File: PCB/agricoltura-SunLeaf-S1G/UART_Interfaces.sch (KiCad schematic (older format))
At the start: 8 parts

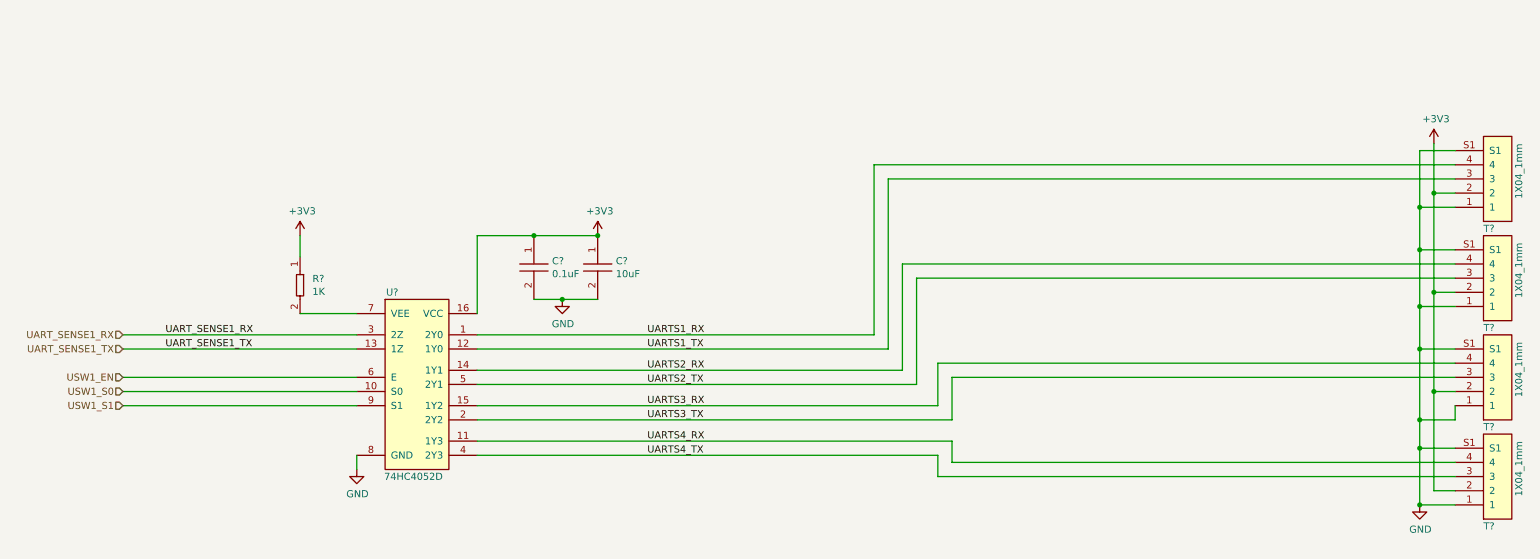
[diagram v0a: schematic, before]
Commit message: Schematic Complete
Schematic completed and PCB started
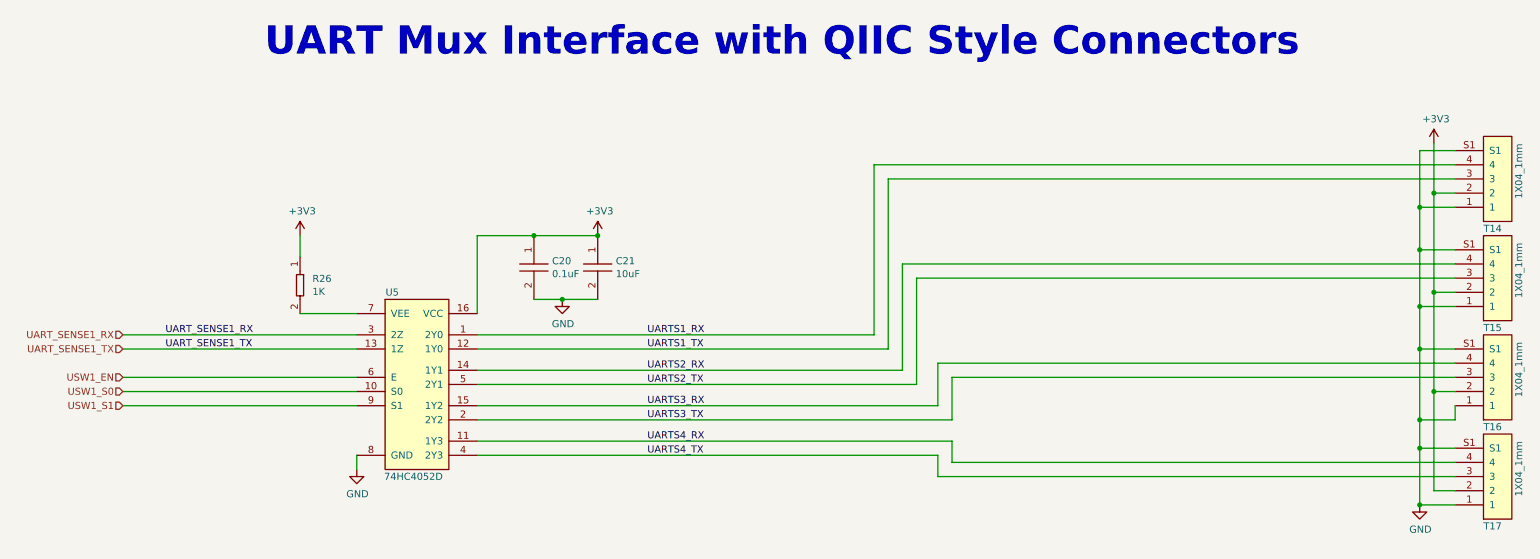
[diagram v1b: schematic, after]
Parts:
- gave numbers to parts that had none: 8
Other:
- note added: "UART Mux Interface with QIIC Style Connectors"
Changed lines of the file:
@@
 $EndDescr
 $Comp
-L AVR-KiCAD-Lib-ICs:74HC4052D U?
+L AVR-KiCAD-Lib-ICs:74HC4052D U5
 U 1 1 5EFDBFF8
 P 3050 3250
-F 0 "U?" H 3100 3300 50  0000 C CNN
+F 0 "U5" H 3100 3300 50  0000 C CNN
 F 1 "74HC4052D" H 3100 3450 50  0001 C CNN
 F 2 "AVR-KiCAD-Lib-ICs:74HC4052D" H 2850 3200 50  0001 C CNN
@@
 AR Path="/5EE82896/5F137C30" Ref="C?"  Part="1"
 AR Path="/5EE82702/5F137C30" Ref="C?"  Part="1"
-AR Path="/5F05538C/5F137C30" Ref="C?"  Part="1"
-F 0 "C?" V 4079 3128 50  0000 L CNN
+AR Path="/5F05538C/5F137C30" Ref="C20"  Part="1"
+F 0 "C20" V 4079 3128 50  0000 L CNN
 F 1 "C0402C104K9PACTU" H 4150 3200 50  0001 C CNN
 F 2 "AVR-KiCAD-Lib-Resistors:R0402" H 3900 3000 50  0001 C CNN
@@
 AR Path="/5EE82896/5F137C4F" Ref="C?"  Part="1"
 AR Path="/5EE82702/5F137C4F" Ref="C?"  Part="1"
-AR Path="/5F05538C/5F137C4F" Ref="C?"  Part="1"
-F 0 "C?" V 4529 3128 50  0000 L CNN
+AR Path="/5F05538C/5F137C4F" Ref="C21"  Part="1"
+F 0 "C21" V 4529 3128 50  0000 L CNN
 F 1 "GRM188R61A106KE69J" H 4600 3200 50  0001 C CNN
 F 2 "AVR-KiCAD-Lib-Capacitors:C0603" H 4350 3000 50  0001 C CNN
@@
 AR Path="/5EE82896/5F137C58" Ref="#PWR?"  Part="1"
 AR Path="/5EE82702/5F137C58" Ref="#PWR?"  Part="1"
-AR Path="/5F05538C/5F137C58" Ref="#PWR?"  Part="1"
-F 0 "#PWR?" H 4550 2650 50  0001 C CNN
+AR Path="/5F05538C/5F137C58" Ref="#PWR036"  Part="1"
+F 0 "#PWR036" H 4550 2650 50  0001 C CNN
 F 1 "+3V3" H 4565 2973 50  0000 C CNN
 F 2 "" H 4550 2800 50  0001 C CNN
@@
 AR Path="/5EE82896/5F137C62" Ref="#PWR?"  Part="1"
 AR Path="/5EE82702/5F137C62" Ref="#PWR?"  Part="1"
-AR Path="/5F05538C/5F137C62" Ref="#PWR?"  Part="1"
-F 0 "#PWR?" H 4300 3000 50  0001 C CNN
+AR Path="/5F05538C/5F137C62" Ref="#PWR035"  Part="1"
+F 0 "#PWR035" H 4300 3000 50  0001 C CNN
 F 1 "GND" H 4305 3077 50  0000 C CNN
 F 2 "" H 4300 3250 50  0001 C CNN
@@
 $EndComp
 $Comp
-L power:GND #PWR?
+L power:GND #PWR034
 U 1 1 5F13C4D0
 P 2850 4450
-F 0 "#PWR?" H 2850 4200 50  0001 C CNN
+F 0 "#PWR034" H 2850 4200 50  0001 C CNN
 F 1 "GND" H 2855 4277 50  0000 C CNN
 F 2 "" H 2850 4450 50  0001 C CNN
@@
 AR Path="/5EE82896/5F151E2B" Ref="#PWR?"  Part="1"
 AR Path="/5EE82702/5F151E2B" Ref="#PWR?"  Part="1"
-AR Path="/5F05538C/5F151E2B" Ref="#PWR?"  Part="1"
-F 0 "#PWR?" H 10450 2000 50  0001 C CNN
+AR Path="/5F05538C/5F151E2B" Ref="#PWR038"  Part="1"
+F 0 "#PWR038" H 10450 2000 50  0001 C CNN
 F 1 "+3V3" H 10465 2323 50  0000 C CNN
 F 2 "" H 10450 2150 50  0001 C CNN
@@
 	3700 4100 7050 4100
 $Comp
-L power:GND #PWR?
+L power:GND #PWR037
 U 1 1 5F0D61E7
 P 10350 4700
-F 0 "#PWR?" H 10350 4450 50  0001 C CNN
+F 0 "#PWR037" H 10350 4450 50  0001 C CNN
 F 1 "GND" H 10355 4527 50  0000 C CNN
 F 2 "" H 10350 4700 50  0001 C CNN
@@
 AR Path="/5EE827B2/5EF0AA2D" Ref="T?"  Part="1"
 AR Path="/5EE82702/5EF0AA2D" Ref="T?"  Part="1"
-AR Path="/5F05538C/5EF0AA2D" Ref="T?"  Part="1"
-F 0 "T?" H 10800 2750 50  0000 L CNN
+AR Path="/5F05538C/5EF0AA2D" Ref="T14"  Part="1"
+F 0 "T14" H 10800 2750 50  0000 L CNN
 F 1 "BM04B-SRSS-TB(LF)(SN)" H 10850 2900 50  0001 C CNN
 F 2 "AVR-KiCAD-Lib-Connectors:CONN_BM04B-SRSS-TB(LF)(SN)" H 9900 3300 50  0001 C CNN
@@
 AR Path="/5EE827B2/5EF0AA4C" Ref="T?"  Part="1"
 AR Path="/5EE82702/5EF0AA4C" Ref="T?"  Part="1"
-AR Path="/5F05538C/5EF0AA4C" Ref="T?"  Part="1"
-F 0 "T?" H 10800 3450 50  0000 L CNN
+AR Path="/5F05538C/5EF0AA4C" Ref="T15"  Part="1"
+F 0 "T15" H 10800 3450 50  0000 L CNN
 F 1 "BM04B-SRSS-TB(LF)(SN)" H 10850 3600 50  0001 C CNN
 F 2 "AVR-KiCAD-Lib-Connectors:CONN_BM04B-SRSS-TB(LF)(SN)" H 9900 4000 50  0001 C CNN
@@
 AR Path="/5EE827B2/5EF0AA6B" Ref="T?"  Part="1"
 AR Path="/5EE82702/5EF0AA6B" Ref="T?"  Part="1"
-AR Path="/5F05538C/5EF0AA6B" Ref="T?"  Part="1"
-F 0 "T?" H 10800 4150 50  0000 L CNN
+AR Path="/5F05538C/5EF0AA6B" Ref="T16"  Part="1"
+F 0 "T16" H 10800 4150 50  0000 L CNN
 F 1 "BM04B-SRSS-TB(LF)(SN)" H 10850 4300 50  0001 C CNN
 F 2 "AVR-KiCAD-Lib-Connectors:CONN_BM04B-SRSS-TB(LF)(SN)" H 9900 4700 50  0001 C CNN
@@
 AR Path="/5EE827B2/5EF0AA8A" Ref="T?"  Part="1"
 AR Path="/5EE82702/5EF0AA8A" Ref="T?"  Part="1"
-AR Path="/5F05538C/5EF0AA8A" Ref="T?"  Part="1"
-F 0 "T?" H 10800 4850 50  0000 L CNN
+AR Path="/5F05538C/5EF0AA8A" Ref="T17"  Part="1"
+F 0 "T17" H 10800 4850 50  0000 L CNN
 F 1 "BM04B-SRSS-TB(LF)(SN)" H 10850 5000 50  0001 C CNN
 F 2 "AVR-KiCAD-Lib-Connectors:CONN_BM04B-SRSS-TB(LF)(SN)" H 9900 5400 50  0001 C CNN
@@
 AR Path="/5EE82896/5F080A60" Ref="R?"  Part="1"
 AR Path="/5EE82702/5F080A60" Ref="R?"  Part="1"
-AR Path="/5F05538C/5F080A60" Ref="R?"  Part="1"
-F 0 "R?" V 2404 3237 50  0000 L CNN
+AR Path="/5F05538C/5F080A60" Ref="R26"  Part="1"
+F 0 "R26" V 2404 3237 50  0000 L CNN
 F 1 "RC0402FR-071KL" V 2450 3238 50  0001 L CNN
 F 2 "AVR-KiCAD-Lib-Resistors:R0402" H 2450 3150 50  0001 C CNN
@@
 AR Path="/5EE82896/5F084046" Ref="#PWR?"  Part="1"
 AR Path="/5EE82702/5F084046" Ref="#PWR?"  Part="1"
-AR Path="/5F05538C/5F084046" Ref="#PWR?"  Part="1"
-F 0 "#PWR?" H 2450 2650 50  0001 C CNN
+AR Path="/5F05538C/5F084046" Ref="#PWR033"  Part="1"
+F 0 "#PWR033" H 2450 2650 50  0001 C CNN
 F 1 "+3V3" H 2465 2973 50  0000 C CNN
 F 2 "" H 2450 2800 50  0001 C CNN
@@
 Wire Wire Line
 	2450 3350 2850 3350
+Text Notes 2200 1550 0    200  ~ 40
+UART Mux Interface with QIIC Style Connectors
 $EndSCHEMATC

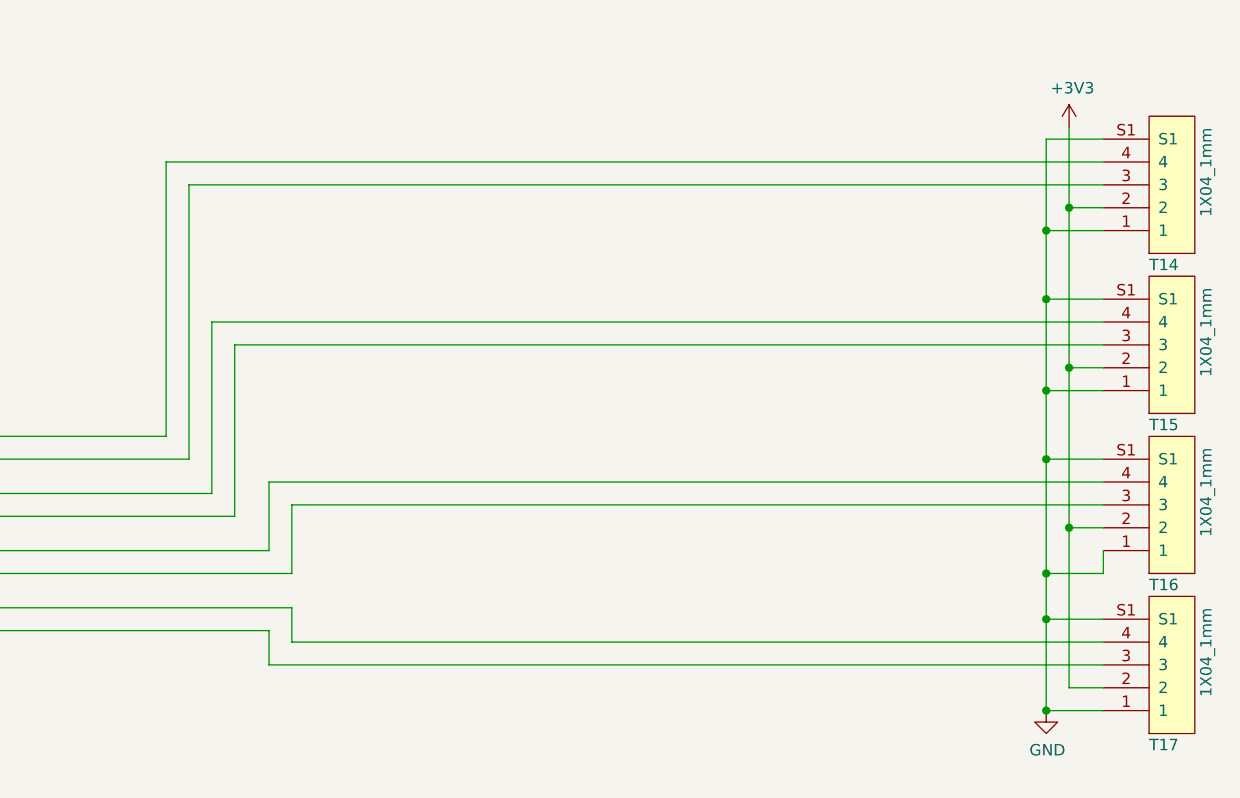
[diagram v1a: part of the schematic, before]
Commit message: PCB Progress
added TVS diodes fo QWIIC connector serial signals. Did more routing overall.
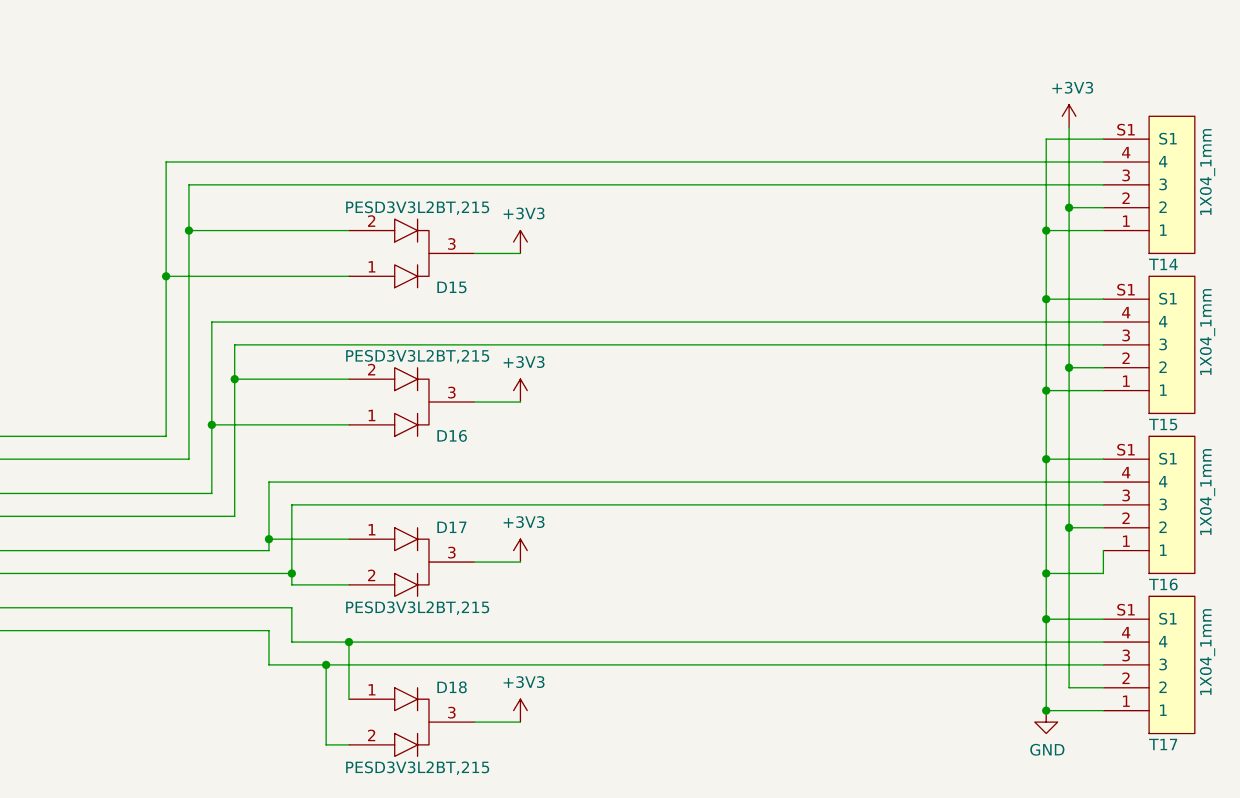
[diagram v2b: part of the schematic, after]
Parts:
- added D15, D16, D17, D18: PESD3V3L2BT,215, AVR-KiCAD-Lib-Diodes:SOT-23, symbol AVR-KiCAD-Lib-Diodes:PESD3V3L2BT,215
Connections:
- net +3V3: now also D15.3, D16.3, D17.3, D18.3
- net UARTS1_RX: now also D15.1
- net UARTS1_TX: now also D15.2
- net UARTS2_RX: now also D16.1
- net UARTS2_TX: now also D16.2
- net UARTS3_RX: now also D17.1
- net UARTS3_TX: now also D17.2
- net UARTS4_RX: now also D18.1
- net UARTS4_TX: now also D18.2
